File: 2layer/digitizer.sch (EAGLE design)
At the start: 23 parts, among them IC1 LT1763CS8-3

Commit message: added some layout
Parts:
- removed IC1: LT1763CS8-3, linear-technology:LT1763CS8-3
- removed Z5: 0, components:L-US0805
- added R5: 25, resistor:R-US_R0402
- added U$4: LT1763CS8-3, linear-technology:LT1763CS8-3
- added X1: SMA-142-0711-881/886, con-coax:SMA-142-0711-881/886
- added Z10, Z3, Z4, Z9: 0, components:L-US0805
- added Z8: 0, resistor:C-USC0402
- Z6: value 0 -> 12p; device components:L-US0805 -> resistor:C-USC0402
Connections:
- net SIG+ renamed MIX+
- net SIG- renamed MIX-
- new net N$1: R5.2, Z6.1, Z9.1
- new net N$10: R5.1, X1.1
- new net RFILT: Z10.1, Z8.1, Z9.2
- new net RFIN: Z10.2
- net AIN+: now also Z3.2
- net AIN-: now also Z4.2
- net AVDD: now also U$4.!SHDN, U$4.IN; no longer IC1.!SHDN, IC1.IN
- net DVDD: now also U$4.OUT, U$4.SENSE; no longer IC1.OUT, IC1.SENSE
- net GND: now also U$4.GND@1, U$4.GND@2, U$4.GND@3, X1.2, Z6.2, Z8.2; no longer IC1.GND@1, IC1.GND@2, IC1.GND@3
- net N$6: now also Z3.1; no longer Z5.1
- net N$7: now also Z4.1; no longer Z6.1
- net N$9: now also U$4.BYP; no longer IC1.BYP
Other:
- note added: "Antenna Matching and IF Bypass"
- moved on the sheet: C1, C10, C11, C2, C3, C4, C5, C6, C7, C8, C9, R1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

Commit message: started layout
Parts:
- added C12: 1u, resistor:C-USC0402
- added C13, C14: 10n, resistor:C-USC0402
- added JP1, JP2: (no value), pinhead:PINHD-1X10
- added R6, R7: 25, resistor:R-US_R0402
- added U$5: LT5560, components:LT5560
- added Z11: 12p, resistor:C-USC0402
- added Z5, Z7: 0, components:L-US0805
- R5: device resistor:R-US_R0402 -> resistor:R-US_R0805
- Z6, Z8: device resistor:C-USC0402 -> resistor:C-USC0805
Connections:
- new net LO+: C13.1
- new net LO-: C14.1
- new net MIXEN: U$5.EN
- new net N$20: C12.1, U$5.VCC
- new net N$21: C14.2, U$5.LO-
- new net N$22: C13.2, U$5.LO+
- new net N$23: R6.2, Z11.1, Z5.1
- new net N$24: U$5.IN+, Z5.2
- new net N$25: U$5.IN-, Z10.2
- new net N$26: R7.2, Z10.1, Z11.2
- new net N$27: R6.1
- new net N$28: R7.1
- new net SDC_OEN: JP2.4
- net ADC_SLP: now also JP2.3
- net GND: now also C12.2, U$5.GND
- net N$1: now also Z7.1; no longer Z9.1
- net OVFL: now also JP2.2
- net RFILT: now also Z7.2, Z9.1; no longer Z10.1, Z9.2
- net RFIN: now also Z9.2; no longer Z10.2
- net SAMP0: now also JP1.1
- net SAMP1: now also JP1.2
- net SAMP2: now also JP1.3
- net SAMP3: now also JP1.4
- net SAMP4: now also JP1.5
- net SAMP5: now also JP1.6
- net SAMP6: now also JP1.7
- net SAMP7: now also JP1.8
- net SAMP8: now also JP1.9
- net SAMP9: now also JP1.10
- net SAMPCLK: now also JP2.1
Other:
- moved on the sheet: Z10, Z9

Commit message: started layout2
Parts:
- removed JP2: (no value), pinhead:PINHD-1X10
- added X2: SMA-142-0711-881/886, con-coax:SMA-142-0711-881/886
- JP1: device pinhead:PINHD-1X10 -> pinhead:PINHD-2X20
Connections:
- removed net SDC_OEN: JP2.4
- net ADC_SLP: no longer JP2.3
- net OVFL: no longer JP2.2
- net SAMP0: no longer JP1.1
- net SAMP1: no longer JP1.2
- net SAMP2: no longer JP1.3
- net SAMP3: no longer JP1.4
- net SAMP4: no longer JP1.5
- net SAMP5: no longer JP1.6
- net SAMP6: no longer JP1.7
- net SAMP7: no longer JP1.8
- net SAMP8: no longer JP1.9
- net SAMP9: no longer JP1.10
- net SAMPCLK: no longer JP2.1

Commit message: starting final layout
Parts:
- added C15: (no value), rcl:C-USC0402
- added C16, C17: 18p, resistor:C-USC0402
- added C18, C19, C21: 0.1u, resistor:C-USC0402
- added C20: 1u, resistor:C-USC0402
- added C22: 4.7u, resistor:C-USC0402
- added IC1: FT601QQFN76, lt_ftdi_and_more:FT601QQFN76
- added JP2: (no value), pinhead:PINHD-2X20
- added JP3: (no value), pinhead:PINHD-1X4
- added R10, R12, R13, R16, R17: (no value), resistor:R-US_R0402
- added R11: (no value), resistor:R-US_V234/12
- added R14, R15: 0, resistor:R-US_R0805
- added S1, S2: MOMENTARY-SWITCH-SPST-SMD-6.0X3.5MM, SparkFun-Switches:MOMENTARY-SWITCH-SPST-SMD-6.0X3.5MM
- added U$6: USB3.0, components:USB3.0
- added U$7: CX3225SB_UKY1C-H1-16357-0045, components:CX3225SB_UKY1C-H1-16357-0045
- Z10, Z3, Z4, Z5: device components:L-US0805 -> components:L-US0402
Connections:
- removed net N$27: R6.1
- removed net N$28: R7.1
- new net BE0: IC1.BE_0
- new net BE1: IC1.BE_1
- new net BE2: IC1.BE_2
- new net BE3: IC1.BE_3
- new net D+: IC1.DP, U$6.D+
- new net D-: IC1.DM, U$6.D-
- new net FCLK: IC1.CLK
- new net GPIO0: IC1.GPIO0
- new net GPIO1: IC1.GPIO1
- new net N$11: C16.2, IC1.XI, U$7.1
- new net N$12: C17.2, IC1.XO, U$7.3
- new net N$13: IC1.RREF, R10.2, R11.2
- new net N$14: C18.2, U$6.SSTX+
- new net N$15: C19.2, U$6.SSTX-
- new net N$16: R14.1, X2.1
- new net OEN: IC1.OE_N
- new net OTG_ID: U$6.ID
- new net RDN: IC1.RD_N
- new net RFIN2: JP3.2, R7.1
- new net RSTN: IC1.RESET_N, R12.2, R17.1, S2.2
- new net RXFN: IC1.RXF_N
- new net SFT_RSTN: R17.2
- new net SFT_WKPN: R16.2
- new net SIWUN: IC1.SIWU_N
- new net SSRX+: IC1.RIDP, U$6.SSRX+
- new net SSRX-: IC1.RIDN, U$6.SSRX-
- new net SSTX+: C18.1, IC1.TODP
- new net SSTX-: C19.1, IC1.TODN
- new net TXEN: IC1.TXE_N
- new net UDAT0: IC1.DATA_0
- new net UDAT1: IC1.DATA_1
- new net UDAT10: IC1.DATA_10
- new net UDAT11: IC1.DATA_11
- new net UDAT12: IC1.DATA_12
- new net UDAT13: IC1.DATA_13
- new net UDAT14: IC1.DATA_14
- new net UDAT15: IC1.DATA_15
- new net UDAT16: IC1.DATA_16
- new net UDAT17: IC1.DATA_17
- new net UDAT18: IC1.DATA_18
- new net UDAT19: IC1.DATA_19
- new net UDAT2: IC1.DATA_2
- new net UDAT20: IC1.DATA_20
- new net UDAT21: IC1.DATA_21
- new net UDAT22: IC1.DATA_22
- new net UDAT23: IC1.DATA_23
- new net UDAT24: IC1.DATA_24
- new net UDAT25: IC1.DATA_25
- new net UDAT26: IC1.DATA_26
- new net UDAT27: IC1.DATA_27
- new net UDAT28: IC1.DATA_28
- new net UDAT29: IC1.DATA_29
- new net UDAT3: IC1.DATA_3
- new net UDAT30: IC1.DATA_30
- new net UDAT31: IC1.DATA_31
- new net UDAT4: IC1.DATA_4
- new net UDAT5: IC1.DATA_5
- new net UDAT6: IC1.DATA_6
- new net UDAT7: IC1.DATA_7
- new net UDAT8: IC1.DATA_8
- new net UDAT9: IC1.DATA_9
- new net V1REF: C15.2, C22.1, IC1.AVDD, IC1.DV10, IC1.VD10, IC1.VD10@1, IC1.VD10@2, IC1.VD10@3
- new net VBUS: IC1.VBUS, U$6.VBUS
- new net WKPN: IC1.WAKEUP_N, R13.2, R16.1, S1.2
- new net WRN: IC1.WR_N
- net AVDD: now also JP3.4, R12.1, R13.1
- net DVDD: now also C20.1, C21.1, IC1.VCC33, IC1.VCC33@1, IC1.VCC33@2, IC1.VCCIO, IC1.VCCIO@1, IC1.VCCIO@2, IC1.VCCIO@3, IC1.VDDA
- net GND: now also C15.1, C16.1, C17.1, C20.2, C21.2, C22.2, IC1.GND, IC1.GND@1, IC1.GND@2, IC1.GND@3, IC1.GND@4, JP3.1, R10.1, R11.1, R15.1, S1.1, S2.1, U$6.GND, U$6.GND-D, U$6.SHEILD1, U$6.SHEILD2, U$7.2, U$7.4, X2.2
- net LO+: now also R14.2
- net LO-: now also R15.2
- net MIX+: now also U$5.OUT+
- net MIX-: now also U$5.OUT-
- net RFIN: now also JP3.3, R6.1
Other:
- note added: "ADC"
- note added: "Analog and Digital power isolation"
- note added: "CHOOSE SWITCH OR FPGA FOR RESET AND WAKEUP SIG"
- note added: "EXTERNAL LO OPTION"
- note added: "Mixer"
- note added: "Stuff only one, dpt on pkg availability"
- moved on the sheet: C1, C10, C11, C12, C13, C14, C2, C3, C4, C5, C6, C7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

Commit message: okawndpam
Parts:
- removed JP3: (no value), pinhead:PINHD-1X4
- removed R14, R15: 0, resistor:R-US_R0805
- removed R5: 25, resistor:R-US_R0805
- removed Z6: 12p, resistor:C-USC0805
- removed Z7, Z9: 0, components:L-US0805
- removed Z8: 0, resistor:C-USC0805
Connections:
- removed net N$16: R14.1, X2.1
- removed net RFILT: Z7.2, Z8.1, Z9.1
- removed net RFIN: JP3.3, R6.1, Z9.2
- removed net RFIN2: JP3.2, R7.1
- net AVDD: no longer JP3.4
- net GND: now also JP1.11, JP1.12, JP1.21, JP1.22, JP1.31, JP2.21, JP2.22, JP2.31, JP2.32; no longer JP3.1, R15.1, X1.2, X2.2, Z6.2, Z8.2
- net LO+: now also X2.1; no longer R14.2
- net LO-: now also X2.2; no longer R15.2
- net N$1: now also R7.1, X1.2; no longer R5.2, Z6.1, Z7.1
- net N$10: now also R6.1; no longer R5.1
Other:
- note removed: "Antenna Matching and IF Bypass"
- moved on the sheet: X1, X2

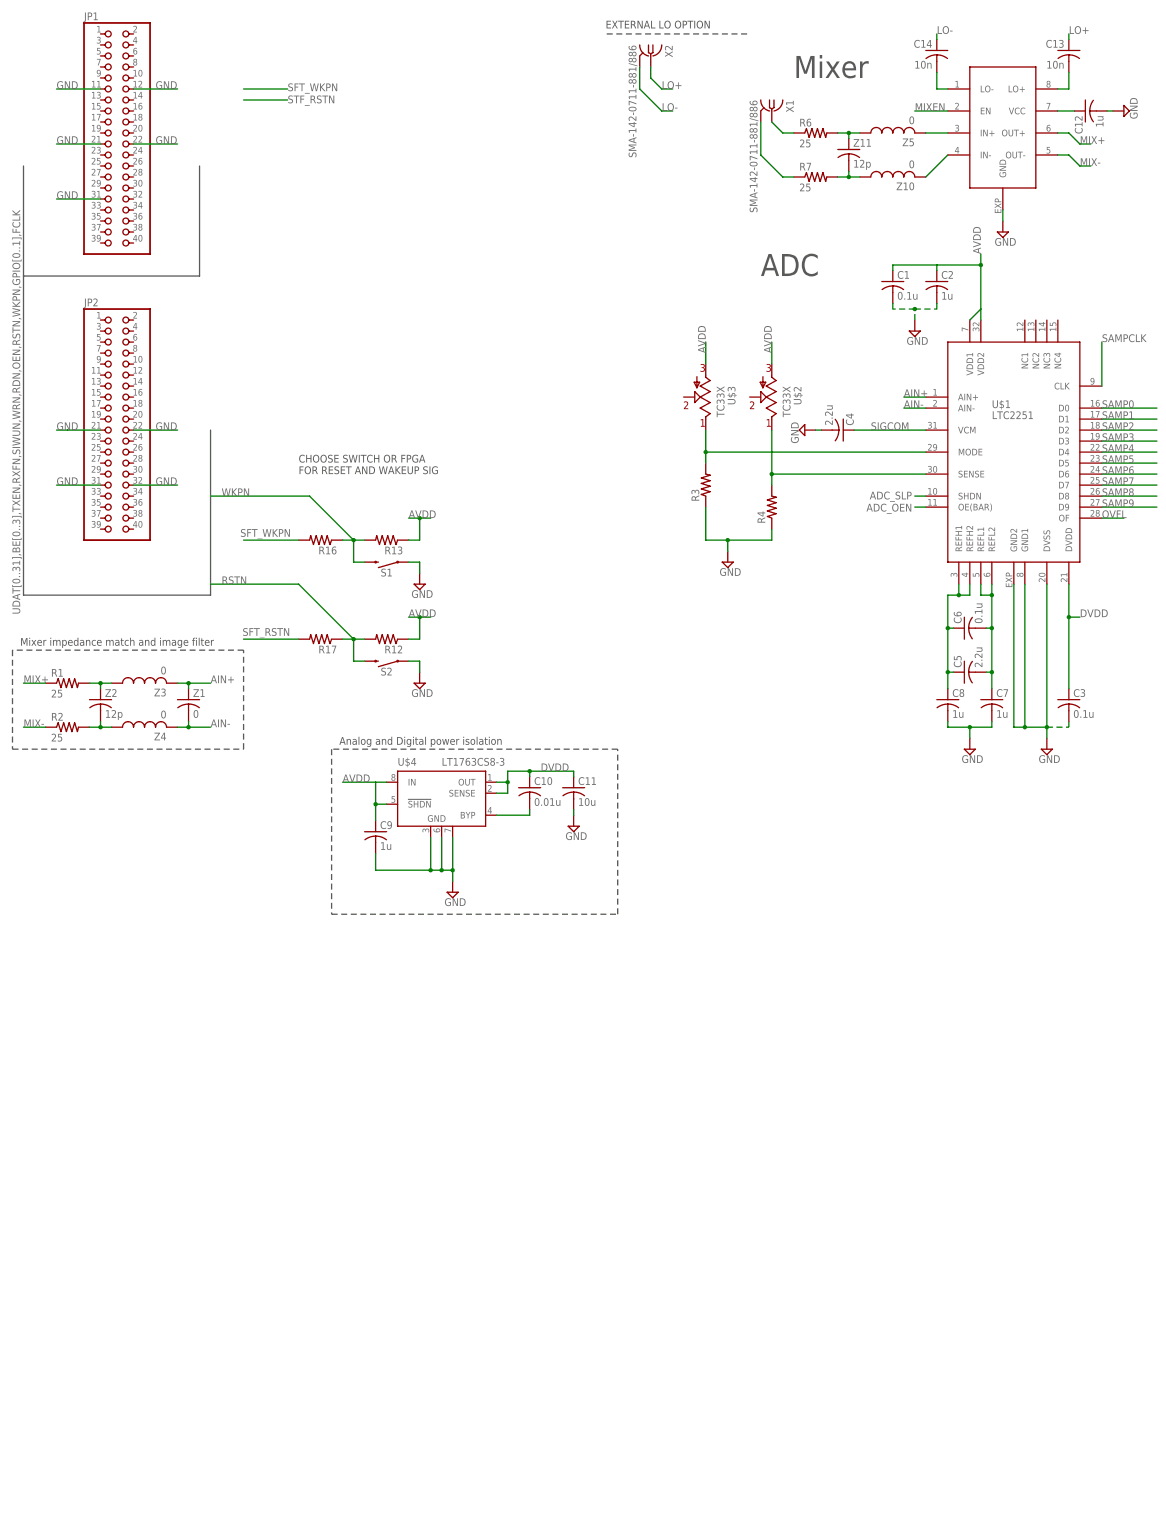
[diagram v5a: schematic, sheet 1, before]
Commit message: moved guts to center to make more of a sheild-like adaptor to mate with MACH
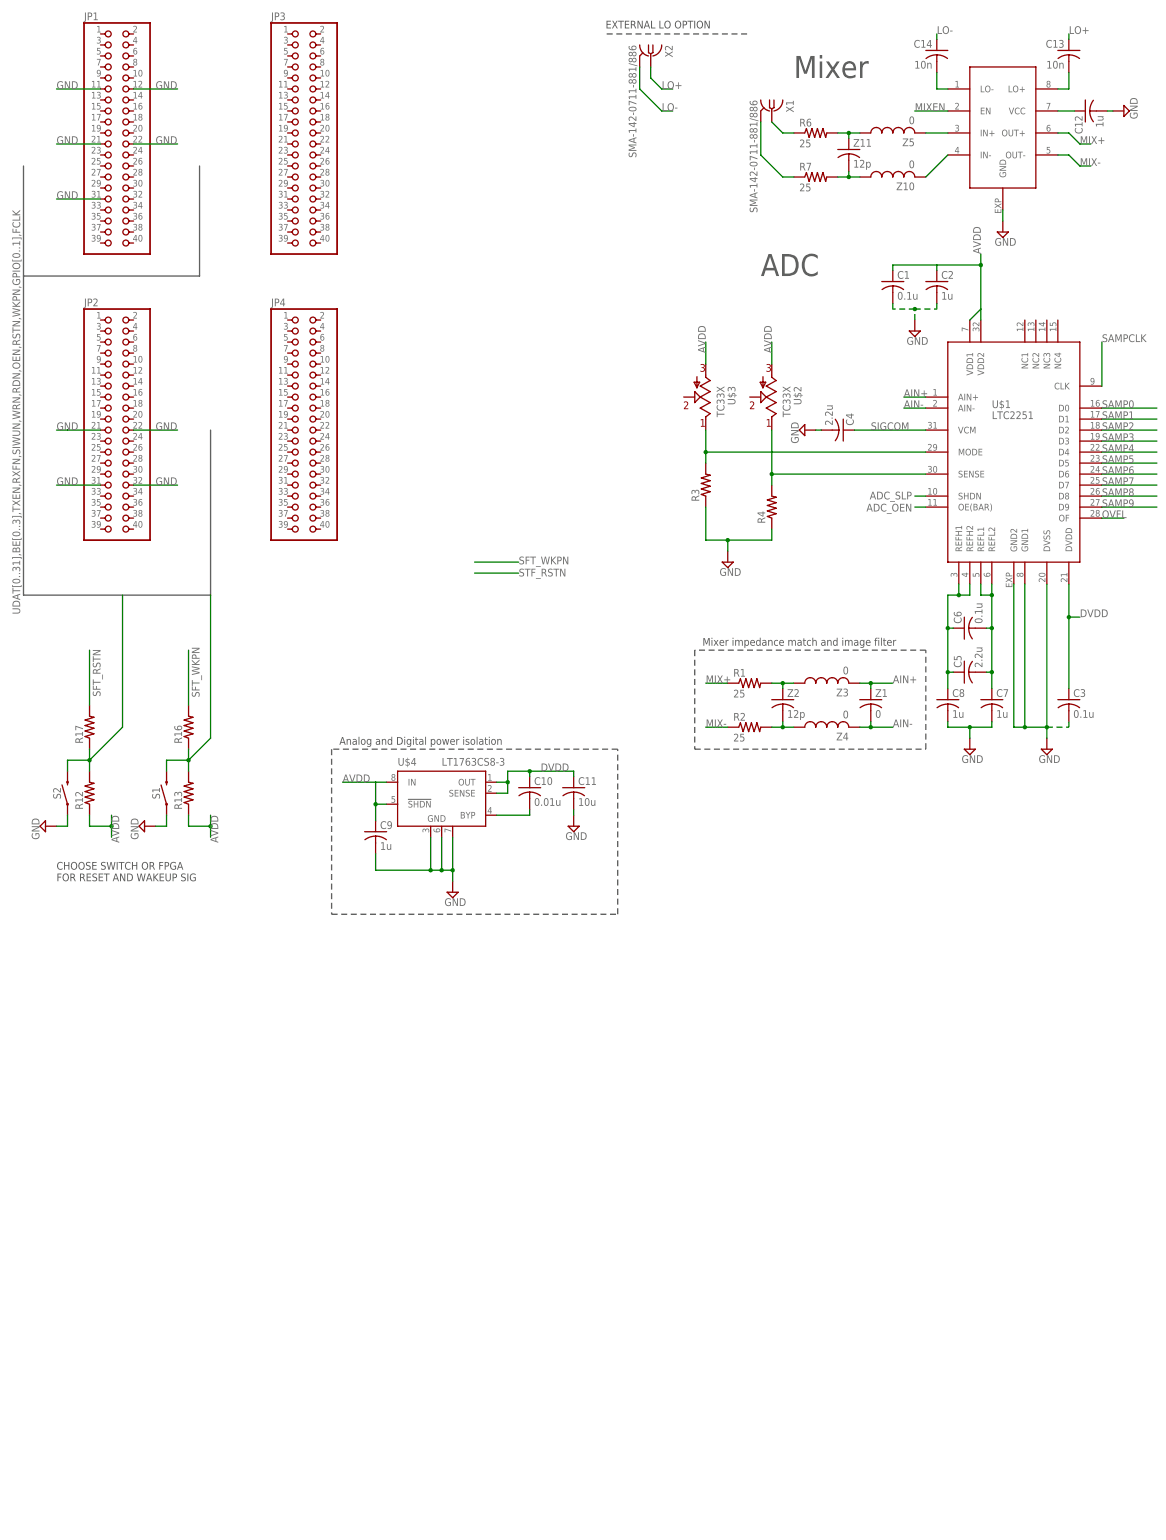
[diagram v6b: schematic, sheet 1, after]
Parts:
- removed R11: (no value), resistor:R-US_V234/12
- added JP3, JP4: (no value), pinhead:PINHD-2X20
- R10: value (none) -> 10k <=0.1%
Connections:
- net GND: no longer R11.1
- net N$13: no longer R11.2
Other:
- note removed: "Stuff only one, dpt on pkg availability"
- moved on the sheet: R1, R10, R12, R13, R16, R17, R2, S1, S2, Z1, Z2, Z3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

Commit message: started meandering fifo bus
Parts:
- renumbered S1 to USB_WAKE, S2 to RESET
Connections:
- new net GND1: JP4.32
- new net GND2: JP4.22
- new net GND3: JP4.12
- new net GND4: JP4.11
- new net GND5: JP4.21
- new net GND6: JP4.31
- net BE0: now also JP4.24
- net BE1: now also JP4.23
- net BE2: now also JP4.26
- net BE3: now also JP4.25
- net FCLK: now also JP1.25
- net GND: now also JP2.11, JP2.12
- net GPIO0: now also JP3.28
- net GPIO1: now also JP3.27
- net OEN: now also JP3.26
- net RDN: now also JP3.25
- net RXFN: now also JP3.21
- net SIWUN: now also JP3.23
- net TXEN: now also JP3.22
- net UDAT0: now also JP2.39
- net UDAT1: now also JP2.40
- net UDAT10: now also JP1.29
- net UDAT11: now also JP1.30
- net UDAT12: now also JP2.28
- net UDAT13: now also JP2.27
- net UDAT14: now also JP1.27
- net UDAT15: now also JP1.28
- net UDAT16: now also JP2.26
- net UDAT17: now also JP2.25
- net UDAT18: now also JP2.24
- net UDAT19: now also JP1.24, JP2.23
- net UDAT2: now also JP2.37
- net UDAT20: now also JP1.23
- net UDAT22: now also JP1.19
- net UDAT23: now also JP1.20
- net UDAT24: now also JP2.20
- net UDAT25: now also JP2.19
- net UDAT26: now also JP2.18
- net UDAT27: now also JP2.17
- net UDAT28: now also JP2.16
- net UDAT29: now also JP2.15
- net UDAT3: now also JP2.38
- net UDAT30: now also JP2.14
- net UDAT31: now also JP2.13
- net UDAT4: now also JP2.35
- net UDAT5: now also JP2.36
- net UDAT6: now also JP2.33
- net UDAT7: now also JP2.34
- net UDAT8: now also JP2.30
- net UDAT9: now also JP2.29
- net WRN: now also JP3.24
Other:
- moved on the sheet: JP3, JP4

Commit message: fixed header positions to match mach
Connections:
- removed net GND1: JP4.32
- removed net GND2: JP4.22
- removed net GND3: JP4.12
- removed net GND4: JP4.11
- removed net GND5: JP4.21
- removed net GND6: JP4.31
- net GND: now also JP3.21, JP3.22, JP4.11, JP4.12, JP4.21, JP4.22, JP4.31, JP4.32
- net RXFN: no longer JP3.21
- net TXEN: no longer JP3.22
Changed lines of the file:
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@@
 <?xml version="1.0" encoding="utf-8"?>
 <!DOCTYPE eagle SYSTEM "eagle.dtd">
-<eagle version="8.0.1">
+<eagle version="8.1.0">
 <drawing>
 <settings>
@@
 <label x="-88.9" y="30.48" size="1.778" layer="95"/>
 </segment>
+<segment>
+<pinref part="JP4" gate="A" pin="12"/>
+<wire x1="-53.34" y1="7.62" x2="-58.42" y2="7.62" width="0.1524" layer="91"/>
+</segment>
+<segment>
+<pinref part="JP4" gate="A" pin="11"/>
+<wire x1="-45.72" y1="7.62" x2="-40.64" y2="7.62" width="0.1524" layer="91"/>
+</segment>
+<segment>
+<pinref part="JP4" gate="A" pin="21"/>
+<wire x1="-45.72" y1="20.32" x2="-40.64" y2="20.32" width="0.1524" layer="91"/>
+</segment>
+<segment>
+<pinref part="JP4" gate="A" pin="22"/>
+<wire x1="-53.34" y1="20.32" x2="-58.42" y2="20.32" width="0.1524" layer="91"/>
+</segment>
+<segment>
+<pinref part="JP4" gate="A" pin="31"/>
+<wire x1="-45.72" y1="33.02" x2="-40.64" y2="33.02" width="0.1524" layer="91"/>
+</segment>
+<segment>
+<pinref part="JP4" gate="A" pin="32"/>
+<wire x1="-53.34" y1="33.02" x2="-58.42" y2="33.02" width="0.1524" layer="91"/>
+</segment>
+<segment>
+<wire x1="-45.72" y1="43.18" x2="-40.64" y2="43.18" width="0.1524" layer="91"/>
+</segment>
+<segment>
+<pinref part="JP3" gate="A" pin="22"/>
+<wire x1="-66.04" y1="86.36" x2="-53.34" y2="86.36" width="0.1524" layer="91"/>
+<label x="-63.5" y="86.36" size="1.778" layer="95"/>
+</segment>
+<segment>
+<pinref part="JP3" gate="A" pin="21"/>
+<wire x1="-30.48" y1="86.36" x2="-45.72" y2="86.36" width="0.1524" layer="91"/>
+<label x="-38.1" y="86.36" size="1.778" layer="95"/>
+</segment>
 </net>
 <net name="AVDD" class="0">
@@
 </segment>
 </net>
-<net name="GND1" class="0">
-<segment>
-<pinref part="JP4" gate="A" pin="32"/>
-<wire x1="-53.34" y1="33.02" x2="-58.42" y2="33.02" width="0.1524" layer="91"/>
-</segment>
-</net>
-<net name="GND2" class="0">
-<segment>
-<pinref part="JP4" gate="A" pin="22"/>
-<wire x1="-53.34" y1="20.32" x2="-58.42" y2="20.32" width="0.1524" layer="91"/>
-</segment>
-</net>
-<net name="GND3" class="0">
-<segment>
-<pinref part="JP4" gate="A" pin="12"/>
-<wire x1="-53.34" y1="7.62" x2="-58.42" y2="7.62" width="0.1524" layer="91"/>
-</segment>
-</net>
-<net name="GND4" class="0">
-<segment>
-<pinref part="JP4" gate="A" pin="11"/>
-<wire x1="-45.72" y1="7.62" x2="-40.64" y2="7.62" width="0.1524" layer="91"/>
-</segment>
-</net>
-<net name="GND5" class="0">
-<segment>
-<pinref part="JP4" gate="A" pin="21"/>
-<wire x1="-45.72" y1="20.32" x2="-40.64" y2="20.32" width="0.1524" layer="91"/>
-</segment>
-</net>
-<net name="GND6" class="0">
-<segment>
-<pinref part="JP4" gate="A" pin="31"/>
-<wire x1="-45.72" y1="33.02" x2="-40.64" y2="33.02" width="0.1524" layer="91"/>
-</segment>
-</net>
-<net name="GND7" class="0">
-<segment>
-<wire x1="-45.72" y1="43.18" x2="-40.64" y2="43.18" width="0.1524" layer="91"/>
-</segment>
-</net>
 <net name="GPIO0" class="0">
 <segment>
@@
 </segment>
 </net>
-<net name="TXEN" class="0">
-<segment>
-<pinref part="JP3" gate="A" pin="22"/>
-<wire x1="-76.2" y1="83.82" x2="-73.66" y2="86.36" width="0.1524" layer="91"/>
-<wire x1="-73.66" y1="86.36" x2="-53.34" y2="86.36" width="0.1524" layer="91"/>
-<label x="-68.58" y="86.36" size="1.778" layer="95"/>
-</segment>
-</net>
-<net name="RXFN" class="0">
-<segment>
-<pinref part="JP3" gate="A" pin="21"/>
-<wire x1="-20.32" y1="83.82" x2="-22.86" y2="86.36" width="0.1524" layer="91"/>
-<wire x1="-22.86" y1="86.36" x2="-45.72" y2="86.36" width="0.1524" layer="91"/>
-<label x="-35.56" y="86.36" size="1.778" layer="95"/>
-</segment>
-</net>
